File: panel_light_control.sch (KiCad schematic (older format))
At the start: 61 parts, among them J1 Conn_01x02, J6 Conn_01x04, Q1 IRF540N, Q2 IRF540N, U1 L7805, U2 LM324, U6 LM324, U7 LM324

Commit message: PHY routing done? Current sink routing is back to square one (yay fwd annotations)
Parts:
- added D4: D, Diode_SMD:D_SMA, symbol Device:D
- D1, D2: footprint Diode_SMD:D_0603_1608Metric -> Diode_SMD:D_SMA; MPN (none) -> CGRA4004-G; Mouser (none) -> 750-CGRA4004-G
- SPI0: value Conn_01x09 -> Conn_01x10; footprint Connector_JST:JST_PH_S9B-PH-K_1x09_P2.00mm_Horizontal -> Connector_JST:JST_PH_S11B-PH-K_1x11_P2.00mm_Horizontal
- renumbered U7 to U2, U6 to U2
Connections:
- wire segments 231 -> 237
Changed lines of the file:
@@
 F 0 "D1" H 3400 1416 50  0000 C CNN
 F 1 "D" H 3400 1325 50  0000 C CNN
-F 2 "Diode_SMD:D_0603_1608Metric" H 3400 1200 50  0001 C CNN
+F 2 "Diode_SMD:D_SMA" H 3400 1200 50  0001 C CNN
 F 3 "~" H 3400 1200 50  0001 C CNN
+F 4 "CGRA4004-G" H 3400 1200 50  0001 C CNN "MPN"
+F 5 "750-CGRA4004-G" H 3400 1200 50  0001 C CNN "Mouser"
 	1    3400 1200
 	1    0    0    -1
@@
 F 0 "D2" H 3400 2400 50  0000 C CNN
 F 1 "D" H 3400 2500 50  0000 C CNN
-F 2 "Diode_SMD:D_0603_1608Metric" H 3400 2600 50  0001 C CNN
+F 2 "Diode_SMD:D_SMA" H 3400 2600 50  0001 C CNN
 F 3 "~" H 3400 2600 50  0001 C CNN
+F 4 "CGRA4004-G" H 3400 2600 50  0001 C CNN "MPN"
+F 5 "750-CGRA4004-G" H 3400 2600 50  0001 C CNN "Mouser"
 	1    3400 2600
 	1    0    0    1
@@
 U 1 1 5C1B802D
 P 4950 1500
-F 0 "U1" H 4950 1742 50  0000 C CNN
-F 1 "L7805" H 4950 1651 50  0000 C CNN
+F 0 "U1" H 5250 1400 50  0000 C CNN
+F 1 "L7805" H 4950 1650 50  0000 C CNN
 F 2 "Package_TO_SOT_THT:TO-220-3_Vertical" H 4975 1350 50  0001 L CIN
 F 3 "http://www.st.com/content/ccc/resource/technical/document/datasheet/41/4f/b3/b0/12/d4/47/88/CD00000444.pdf/files/CD00000444.pdf/jcr:content/translations/en.CD00000444.pdf" H 4950 1450 50  0001 C CNN
@@
 $EndComp
 Wire Wire Line
-	3950 1500 4650 1500
+	3950 1500 4550 1500
 $Comp
 L power:GND #PWR0101
@@
 	5350 1500 5250 1500
 Wire Wire Line
-	5650 1500 5350 1500
+	5650 1500 5550 1500
 Connection ~ 5350 1500
 Text GLabel 10250 2950 0    50   Output ~ 0
@@
 P 10600 4900
 F 0 "SPI0" H 10680 4892 50  0000 L CNN
-F 1 "Conn_01x09" H 10680 4801 50  0000 L CNN
-F 2 "Connector_JST:JST_PH_S9B-PH-K_1x09_P2.00mm_Horizontal" H 10600 4900 50  0001 C CNN
+F 1 "Conn_01x10" H 10680 4801 50  0000 L CNN
+F 2 "Connector_JST:JST_PH_S11B-PH-K_1x11_P2.00mm_Horizontal" H 10600 4900 50  0001 C CNN
 F 3 "~" H 10600 4900 50  0001 C CNN
 	1    10600 4900
@@
 L power:PWR_FLAG #FLG0104
 U 1 1 5C1C5DD8
-P 5350 1400
-F 0 "#FLG0104" H 5350 1475 50  0001 C CNN
-F 1 "PWR_FLAG" H 5350 1574 50  0000 C CNN
-F 2 "" H 5350 1400 50  0001 C CNN
-F 3 "~" H 5350 1400 50  0001 C CNN
-	1    5350 1400
-	1    0    0    -1
-$EndComp
-Wire Wire Line
-	5350 1400 5350 1500
+P 5550 1400
+F 0 "#FLG0104" H 5550 1475 50  0001 C CNN
+F 1 "PWR_FLAG" H 5550 1574 50  0000 C CNN
+F 2 "" H 5550 1400 50  0001 C CNN
+F 3 "~" H 5550 1400 50  0001 C CNN
+	1    5550 1400
+	1    0    0    -1
+$EndComp
 Wire Wire Line
 	2800 1500 2800 2600
@@
 	8950 4500 8950 4600
 $Comp
-L Amplifier_Operational:LM324 U7
-U 2 1 5CE1E150
+L Amplifier_Operational:LM324 U2
+U 3 1 5CE1E150
 P 7750 5400
-F 0 "U7" H 7750 5600 50  0000 C CNN
+F 0 "U2" H 7750 5600 50  0000 C CNN
 F 1 "LM324" H 7700 5400 50  0000 C CNN
 F 2 "Package_DIP:DIP-14_W7.62mm_Socket" H 7700 5500 50  0001 C CNN
 F 3 "http://www.ti.com/lit/ds/symlink/lm2902-n.pdf" H 7800 5600 50  0001 C CNN
-	2    7750 5400
+	3    7750 5400
 	1    0    0    -1
 $EndComp
@@
 	8950 6100 8950 6200
 $Comp
-L Amplifier_Operational:LM324 U6
-U 2 1 5CE38662
+L Amplifier_Operational:LM324 U2
+U 1 1 5CE38662
 P 7750 2250
-F 0 "U6" H 7750 2450 50  0000 C CNN
+F 0 "U2" H 7750 2450 50  0000 C CNN
 F 1 "LM324" H 7700 2250 50  0000 C CNN
 F 2 "Package_DIP:DIP-14_W7.62mm_Socket" H 7700 2350 50  0001 C CNN
 F 3 "http://www.ti.com/lit/ds/symlink/lm2902-n.pdf" H 7800 2450 50  0001 C CNN
-	2    7750 2250
+	1    7750 2250
 	1    0    0    -1
 $EndComp
@@
 Wire Wire Line
 	8950 2950 8950 3050
+Wire Wire Line
+	5550 1400 5550 1500
+Connection ~ 5550 1500
+Wire Wire Line
+	5550 1500 5350 1500
+Wire Wire Line
+	4800 1200 4550 1200
+Wire Wire Line
+	4550 1200 4550 1500
+Connection ~ 4550 1500
+Wire Wire Line
+	4550 1500 4650 1500
+Wire Wire Line
+	5100 1200 5350 1200
+Wire Wire Line
+	5350 1200 5350 1500
+$Comp
+L Device:D D4
+U 1 1 5BD4F72E
+P 4950 1200
+F 0 "D4" H 4950 1416 50  0000 C CNN
+F 1 "D" H 4950 1325 50  0000 C CNN
+F 2 "Diode_SMD:D_SMA" H 4950 1200 50  0001 C CNN
+F 3 "~" H 4950 1200 50  0001 C CNN
+F 4 "CGRA4004-G" H 4950 1200 50  0001 C CNN "MPN"
+F 5 "750-CGRA4004-G" H 4950 1200 50  0001 C CNN "Mouser"
+	1    4950 1200
+	1    0    0    -1
+$EndComp
 $EndSCHEMATC

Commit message: further re-arrangement, PCB is now 100x90 mm² \o/. A bit more placement to do, then back to routing :>
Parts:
- removed C13, C14: 4.7uF, Capacitor_SMD:C_1206_3216Metric, symbol Device:C
- removed C2: 100nF, Capacitor_SMD:C_0603_1608Metric, symbol Device:C
- removed D3: D_Small, Diode_SMD:D_0603_1608Metric, symbol Device:D_Small
- added C25, C41, C42, C43: 22µF, Capacitor_SMD:C_1210_3225Metric, symbol Device:C
- added C38, C39, C40: 100nF, Capacitor_SMD:C_0603_1608Metric, symbol Device:C
- added D3: 1D4004, Diode_SMD:D_SMA, symbol Device:D
- added L2, L3: 4.7µH, Inductor_SMD:L_Taiyo-Yuden_NR-50xx, symbol Device:L
- C3: value 47uF -> 22µF; footprint Capacitor_SMD:C_0603_1608Metric -> Capacitor_SMD:C_1210_3225Metric; MPN (none) -> GMK325BJ226MM-P; Mouser (none) -> 963-GMK325BJ226MM-P
- D1, D2, D4: value D -> 1D4004
- PS1: Mouser (none) -> 919-R-78B12-2.0
- PS2: Arrow Part Number R-78B5.0-1.0 -> (none); Arrow Price/Stock https://www.arrow.com/en/products/r-78b5.0-1.0/recom-power -> (none); Description Switching Regulator R-78B5.0-1.0, 5V 1A Switching Regulator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 -> Non-Isolated DC/DC Converters 1A DC/DC REG 4.75-34Vin 3.3Vou; MPN (none) -> R-78B3.3-1.0; Manufacturer_Name RECOM Power -> (none); Manufacturer_Part_Number R-78B5.0-1.0 -> (none); Mouser (none) -> 919-R-78B3.3-1.0; RS Part Number 1668746 -> (none); RS Price/Stock http://uk.rs-online.com/web/p/products/1668746 -> (none)
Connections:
- wire segments 237 -> 252
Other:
- moved on the sheet: C12, C3, C6, C7, D1, D2, D4, F1, J1, PS1, PS2, PS3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

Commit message: Tweaked MOSFET sink layout. Changed LM324 to SOIC.
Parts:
- U2: footprint Package_DIP:DIP-14_W7.62mm_Socket -> Package_SO:SOIC-14_3.9x8.7mm_P1.27mm
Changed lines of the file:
@@
 EESchema Schematic File Version 4
 LIBS:panel_light_control-cache
-EELAYER 28 0
+EELAYER 26 0
 EELAYER END
 $Descr A4 11693 8268
@@
 F 0 "U2" H 8408 1046 50  0000 L CNN
 F 1 "LM324" H 8408 955 50  0000 L CNN
-F 2 "Package_DIP:DIP-14_W7.62mm_Socket" H 8400 1100 50  0001 C CNN
+F 2 "Package_SO:SOIC-14_3.9x8.7mm_P1.27mm" H 8400 1100 50  0001 C CNN
 F 3 "http://www.ti.com/lit/ds/symlink/lm2902-n.pdf" H 8500 1200 50  0001 C CNN
 	5    8450 1000
@@
 F 0 "U2" H 7750 1300 50  0000 C CNN
 F 1 "LM324" H 7700 1100 50  0000 C CNN
-F 2 "Package_DIP:DIP-14_W7.62mm_Socket" H 7700 1200 50  0001 C CNN
+F 2 "Package_SO:SOIC-14_3.9x8.7mm_P1.27mm" H 7700 1200 50  0001 C CNN
 F 3 "http://www.ti.com/lit/ds/symlink/lm2902-n.pdf" H 7800 1300 50  0001 C CNN
 	4    7750 1100
@@
 F 0 "U2" H 7750 4000 50  0000 C CNN
 F 1 "LM324" H 7700 3800 50  0000 C CNN
-F 2 "Package_DIP:DIP-14_W7.62mm_Socket" H 7700 3900 50  0001 C CNN
+F 2 "Package_SO:SOIC-14_3.9x8.7mm_P1.27mm" H 7700 3900 50  0001 C CNN
 F 3 "http://www.ti.com/lit/ds/symlink/lm2902-n.pdf" H 7800 4000 50  0001 C CNN
 	2    7750 3800
@@
 F 0 "U2" H 7750 5600 50  0000 C CNN
 F 1 "LM324" H 7700 5400 50  0000 C CNN
-F 2 "Package_DIP:DIP-14_W7.62mm_Socket" H 7700 5500 50  0001 C CNN
+F 2 "Package_SO:SOIC-14_3.9x8.7mm_P1.27mm" H 7700 5500 50  0001 C CNN
 F 3 "http://www.ti.com/lit/ds/symlink/lm2902-n.pdf" H 7800 5600 50  0001 C CNN
 	3    7750 5400
@@
 F 0 "U2" H 7750 2450 50  0000 C CNN
 F 1 "LM324" H 7700 2250 50  0000 C CNN
-F 2 "Package_DIP:DIP-14_W7.62mm_Socket" H 7700 2350 50  0001 C CNN
+F 2 "Package_SO:SOIC-14_3.9x8.7mm_P1.27mm" H 7700 2350 50  0001 C CNN
 F 3 "http://www.ti.com/lit/ds/symlink/lm2902-n.pdf" H 7800 2450 50  0001 C CNN
 	1    7750 2250
@@
 Connection ~ 2600 2300
 $Comp
-L power:GND #PWR?
+L power:GND #PWR0113
 U 1 1 5C2605FC
 P 7100 4650
-F 0 "#PWR?" H 7100 4400 50  0001 C CNN
+F 0 "#PWR0113" H 7100 4400 50  0001 C CNN
 F 1 "GND" H 7105 4477 50  0000 C CNN
 F 2 "" H 7100 4650 50  0001 C CNN

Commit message: Add LEDs, tweak MOSFET sink.
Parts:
- R17, R18, R6: footprint Resistor_SMD:R_0603_1608Metric -> Resistor_SMD:R_1206_3216Metric
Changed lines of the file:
@@
 F 0 "R17" H 9150 4400 50  0000 C CNN
 F 1 "0.22" H 9150 4300 50  0000 C CNN
-F 2 "Resistor_SMD:R_0603_1608Metric" V 8880 4350 50  0001 C CNN
+F 2 "Resistor_SMD:R_1206_3216Metric" V 8880 4350 50  0001 C CNN
 F 3 "~" H 8950 4350 50  0001 C CNN
 	1    8950 4350
@@
 F 0 "R18" H 9150 6000 50  0000 C CNN
 F 1 "0.22" H 9150 5900 50  0000 C CNN
-F 2 "Resistor_SMD:R_0603_1608Metric" V 8880 5950 50  0001 C CNN
+F 2 "Resistor_SMD:R_1206_3216Metric" V 8880 5950 50  0001 C CNN
 F 3 "~" H 8950 5950 50  0001 C CNN
 	1    8950 5950
@@
 F 0 "R6" H 9150 2850 50  0000 C CNN
 F 1 "0.22" H 9150 2750 50  0000 C CNN
-F 2 "Resistor_SMD:R_0603_1608Metric" V 8880 2800 50  0001 C CNN
+F 2 "Resistor_SMD:R_1206_3216Metric" V 8880 2800 50  0001 C CNN
 F 3 "~" H 8950 2800 50  0001 C CNN
 	1    8950 2800
@@
 	4600 1200 4300 1200
 Connection ~ 2600 2300
-$Comp
-L power:GND #PWR0113
-U 1 1 5C2605FC
-P 7100 4650
-F 0 "#PWR0113" H 7100 4400 50  0001 C CNN
-F 1 "GND" H 7105 4477 50  0000 C CNN
-F 2 "" H 7100 4650 50  0001 C CNN
-F 3 "" H 7100 4650 50  0001 C CNN
-	1    7100 4650
-	1    0    0    -1
-$EndComp
-Wire Wire Line
-	7100 4550 7100 4650
 Wire Wire Line
 	1700 1200 2000 1200

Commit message: 3.3V buck converter now connected to 12V (prep for 48V>12V upgrade regarding IoP applicability)
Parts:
- added D5: LED_SYSTEM, LED_SMD:LED_Cree-PLCC4_2x2mm_CW, symbol Device:LED_RCBG
- added R39: 220R, Resistor_SMD:R_0603_1608Metric, symbol Device:R_Small
- added R40, R41: 1k, Resistor_SMD:R_0603_1608Metric, symbol Device:R_Small
- F1: value Polyfuse_Small -> Polyfuse 3A; footprint Fuse:Fuse_2512_6332Metric -> SamacSys_Parts:30R400UF; MPN (none) -> 30R300UU; Mouser (none) -> 576-30R300UU
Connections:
- net +12V: now also L2.1
- net +24V: no longer L2.1
- net GND: now also D5.2 (K)
- net PWM_B: now also R39.2
- net PWM_G: now also R40.2
- net PWM_R: now also R41.2
- new net: D5.1 (RA), R41.1
- new net: D5.3 (BA), R39.1
- new net: D5.4 (GA), R40.1
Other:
- moved on the sheet: C39, C41, C7, D2, L2, PS2, PS3, PS4

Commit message: two sections left to place: 3ch current sink, microcontroller area. Todo: * find proper barrel jacks, spec MPN, Mouser * add status LEDs to the LDD-H outputs * add 7th LED for funsies :> * swap LM324 units around until everything lines up best
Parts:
- U2: MPN (none) -> LM324ADR; Mouser (none) -> 595-LM324ADR
- renumbered G3 to Q3
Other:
- moved on the sheet: L3
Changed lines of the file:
@@
 F 2 "Package_SO:SOIC-14_3.9x8.7mm_P1.27mm" H 7700 1200 50  0001 C CNN
 F 3 "http://www.ti.com/lit/ds/symlink/lm2902-n.pdf" H 7800 1300 50  0001 C CNN
+F 4 "LM324ADR" H 7750 1100 50  0001 C CNN "MPN"
+F 5 "595-LM324ADR" H 7750 1100 50  0001 C CNN "Mouser"
 	4    7750 1100
 	1    0    0    -1
@@
 F 2 "Package_SO:SOIC-14_3.9x8.7mm_P1.27mm" H 7700 3900 50  0001 C CNN
 F 3 "http://www.ti.com/lit/ds/symlink/lm2902-n.pdf" H 7800 4000 50  0001 C CNN
+F 4 "LM324ADR" H 7750 3800 50  0001 C CNN "MPN"
+F 5 "595-LM324ADR" H 7750 3800 50  0001 C CNN "Mouser"
 	2    7750 3800
 	1    0    0    -1
@@
 F 2 "Package_SO:SOIC-14_3.9x8.7mm_P1.27mm" H 7700 5500 50  0001 C CNN
 F 3 "http://www.ti.com/lit/ds/symlink/lm2902-n.pdf" H 7800 5600 50  0001 C CNN
+F 4 "LM324ADR" H 7750 5400 50  0001 C CNN "MPN"
+F 5 "595-LM324ADR" H 7750 5400 50  0001 C CNN "Mouser"
 	3    7750 5400
 	1    0    0    -1
@@
 $EndComp
 $Comp
-L Transistor_FET:IRF540N G3
+L Transistor_FET:IRF540N Q3
 U 1 1 5CE1E180
 P 8850 5400
-F 0 "G3" H 9055 5446 50  0000 L CNN
+F 0 "Q3" H 9055 5446 50  0000 L CNN
 F 1 "IRF540N" H 9055 5355 50  0000 L CNN
 F 2 "Package_TO_SOT_THT:TO-220-3_Vertical" H 9100 5325 50  0001 L CIN
@@
 F 2 "Package_SO:SOIC-14_3.9x8.7mm_P1.27mm" H 7700 2350 50  0001 C CNN
 F 3 "http://www.ti.com/lit/ds/symlink/lm2902-n.pdf" H 7800 2450 50  0001 C CNN
+F 4 "LM324ADR" H 7750 2250 50  0001 C CNN "MPN"
+F 5 "595-LM324ADR" H 7750 2250 50  0001 C CNN "Mouser"
 	1    7750 2250
 	1    0    0    -1
@@
 $EndComp
 Wire Wire Line
-	2950 1200 3000 1200
+	2800 1200 3000 1200
 $Comp
 L Device:C C42
@@
 L Device:L L3
 U 1 1 5BFEC541
-P 2800 1200
-F 0 "L3" V 2990 1200 50  0000 C CNN
-F 1 "4.7µH" V 2899 1200 50  0000 C CNN
-F 2 "Inductor_SMD:L_Taiyo-Yuden_NR-50xx" H 2800 1200 50  0001 C CNN
-F 3 "~" H 2800 1200 50  0001 C CNN
-F 4 "VLS5045EX-4R7M-CA " H 2800 1200 50  0001 C CNN "MPN"
-F 5 "810-VLS5045EX4R7MCA" H 2800 1200 50  0001 C CNN "Mouser"
-	1    2800 1200
+P 2650 1200
+F 0 "L3" V 2840 1200 50  0000 C CNN
+F 1 "4.7µH" V 2749 1200 50  0000 C CNN
+F 2 "Inductor_SMD:L_Taiyo-Yuden_NR-50xx" H 2650 1200 50  0001 C CNN
+F 3 "~" H 2650 1200 50  0001 C CNN
+F 4 "VLS5045EX-4R7M-CA " H 2650 1200 50  0001 C CNN "MPN"
+F 5 "810-VLS5045EX4R7MCA" H 2650 1200 50  0001 C CNN "Mouser"
+	1    2650 1200
 	0    -1   -1   0
 $EndComp
@@
 	1700 1700 2000 1700
 Wire Wire Line
-	2300 1200 2650 1200
+	2300 1200 2500 1200
 Text GLabel 2800 2350 0    50   Input ~ 0
 +12V

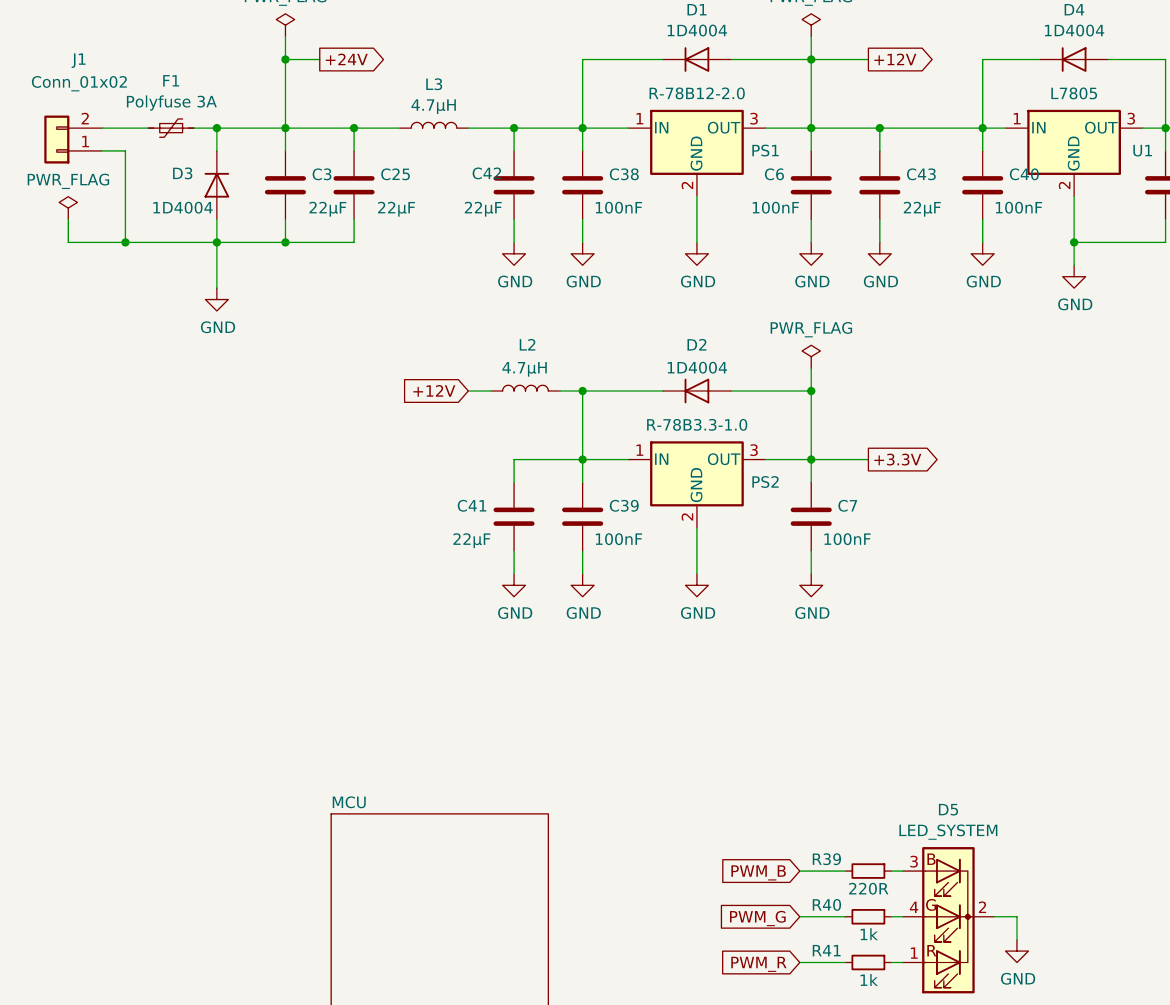
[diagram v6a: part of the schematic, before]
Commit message: THT pad restring sizes increase for mechanical stability; generalized LED arrangement for more flexibility (8 bit display, CAN LED, PWM and general purpose RGB) and development-style look and feel; protection diode footprint is now THT to reduce reworking hassle should it short out due to misuse
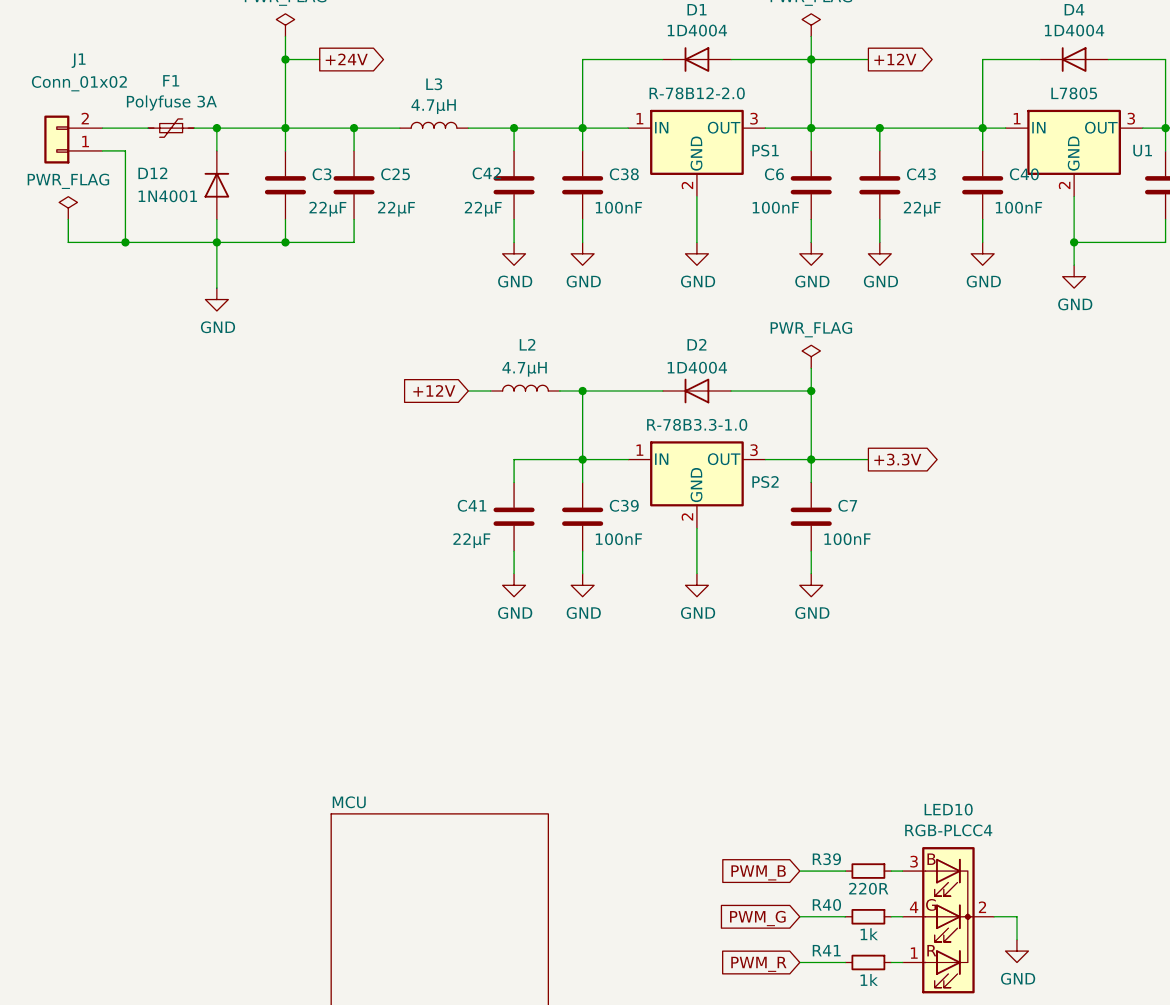
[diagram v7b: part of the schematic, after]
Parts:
- removed D3: 1D4004, Diode_SMD:D_SMA, symbol Device:D
- added D12: 1N4001, Diode_THT:D_DO-41_SOD81_P3.81mm_Vertical_AnodeUp, symbol Diode:1N4001
- LED10: renamed from D5; value LED_SYSTEM -> RGB-PLCC4
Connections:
- net +24V: now also D12.1 (K)
- net GND: now also D12.2 (A)
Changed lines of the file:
@@
 	1    0    0    -1
-$EndComp
-$Comp
-L Device:D D3
-U 1 1 5BDA8380
-P 1700 1450
-F 0 "D3" V 1650 1600 50  0000 C CNN
-F 1 "1D4004" V 1800 1600 50  0000 C CNN
-F 2 "Diode_SMD:D_SMA" H 1700 1450 50  0001 C CNN
-F 3 "~" H 1700 1450 50  0001 C CNN
-F 4 "CGRA4004-G" H 1700 1450 50  0001 C CNN "MPN"
-F 5 "750-CGRA4004-G" H 1700 1450 50  0001 C CNN "Mouser"
-	1    1700 1450
-	0    -1   1    0
 $EndComp
 Wire Wire Line
@@
 P 4900 4650
 AR Path="/5BBC4BB7/5BE88702" Ref="D?"  Part="1"
-AR Path="/5BE88702" Ref="D5"  Part="1"
-F 0 "D5" H 4900 4183 50  0000 C CNN
-F 1 "LED_SYSTEM" H 4900 4274 50  0000 C CNN
+AR Path="/5BE88702" Ref="LED10"  Part="1"
+F 0 "LED10" H 4900 4183 50  0000 C CNN
+F 1 "RGB-PLCC4" H 4900 4274 50  0000 C CNN
 F 2 "LED_SMD:LED_Cree-PLCC4_2x2mm_CW" H 4900 4600 50  0001 C CNN
 F 3 "~" H 4900 4600 50  0001 C CNN
@@
 Text GLabel 4250 4450 0    50   Input ~ 0
 PWM_B
+$Comp
+L Diode:1N4001 D12
+U 1 1 5BD0EDAE
+P 1700 1450
+F 0 "D12" V 1650 1800 50  0000 R CNN
+F 1 "1N4001" V 1750 1800 50  0000 R CNN
+F 2 "Diode_THT:D_DO-41_SOD81_P3.81mm_Vertical_AnodeUp" H 1700 1275 50  0001 C CNN
+F 3 "http://www.vishay.com/docs/88503/1n4001.pdf" H 1700 1450 50  0001 C CNN
+	1    1700 1450
+	0    -1   1    0
+$EndComp
 $EndSCHEMATC

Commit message: R-78B3.3 footprint fixed (had the E version -> mirrored), next: place remaining current sink circuit parts, route upper half of the PCB, tidy up CAN placement, verify µC pin mapping again, route lower half :)
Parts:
- PS2: footprint Converter_DCDC:Converter_DCDC_RECOM_R-78E-0.5_THT -> Converter_DCDC:Converter_DCDC_RECOM_R-78B-2.0_THT; symbol Regulator_Switching:R-783.3-1.0 -> Regulator_Switching:R-78B3.3-2.0
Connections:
- net GND: now also U2.10 (+); no longer U2.12 (+)
- net at C8.2, R7.1, R8.1: now also U2.3 (+); no longer U2.5 (+)
- net at C10.2, R11.1, R14.1: now also U2.2 (-); no longer U2.6 (-)
- net at C10.1, R13.2: now also U2.1; no longer U2.7
- net at C9.2, R10.1, R9.1: now also U2.5 (+); no longer U2.10 (+)
- net at C11.1, R15.2: now also U2.7; no longer U2.8
- net at C11.2, R12.1, R16.1: now also U2.6 (-); no longer U2.9 (-)
- net at C4.1, R4.2: now also U2.14; no longer U2.1
- net at C4.2, R3.1, R5.1: now also U2.13 (-); no longer U2.2 (-)
- net at C1.2, R1.1, R2.1: now also U2.12 (+); no longer U2.3 (+)
- new net: U2.8, U2.9 (-)
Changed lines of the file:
@@
 $EndComp
 $Comp
-L Regulator_Switching:R-783.3-1.0 PS2
+L Regulator_Switching:R-78B3.3-2.0 PS2
 U 1 1 5BB90449
 P 3800 2650
 F 0 "PS2" H 4100 2550 50  0000 C CNN
 F 1 "R-78B3.3-1.0" H 3800 2800 50  0000 C CNN
-F 2 "Converter_DCDC:Converter_DCDC_RECOM_R-78E-0.5_THT" H 4850 2750 50  0001 L CNN
+F 2 "Converter_DCDC:Converter_DCDC_RECOM_R-78B-2.0_THT" H 4850 2750 50  0001 L CNN
 F 3 "" H 4850 2650 50  0001 L CNN
 F 4 "Non-Isolated DC/DC Converters 1A DC/DC REG 4.75-34Vin 3.3Vou" H 4850 2550 50  0001 L CNN "Description"
@@
 $Comp
 L Amplifier_Operational:LM324 U2
-U 4 1 5BC3AA2E
+U 3 1 5BC3AA2E
 P 7750 1100
 F 0 "U2" H 7750 1300 50  0000 C CNN
@@
 F 4 "LM324ADR" H 7750 1100 50  0001 C CNN "MPN"
 F 5 "595-LM324ADR" H 7750 1100 50  0001 C CNN "Mouser"
-	4    7750 1100
+	3    7750 1100
 	1    0    0    -1
 $EndComp
@@
 $Comp
 L Amplifier_Operational:LM324 U2
-U 2 1 5BCB6EE3
+U 1 1 5BCB6EE3
 P 7750 3800
 F 0 "U2" H 7750 4000 50  0000 C CNN
@@
 F 4 "LM324ADR" H 7750 3800 50  0001 C CNN "MPN"
 F 5 "595-LM324ADR" H 7750 3800 50  0001 C CNN "Mouser"
-	2    7750 3800
+	1    7750 3800
 	1    0    0    -1
 $EndComp
@@
 $Comp
 L Amplifier_Operational:LM324 U2
-U 3 1 5CE1E150
+U 2 1 5CE1E150
 P 7750 5400
 F 0 "U2" H 7750 5600 50  0000 C CNN
@@
 F 4 "LM324ADR" H 7750 5400 50  0001 C CNN "MPN"
 F 5 "595-LM324ADR" H 7750 5400 50  0001 C CNN "Mouser"
-	3    7750 5400
+	2    7750 5400
 	1    0    0    -1
 $EndComp
@@
 $Comp
 L Amplifier_Operational:LM324 U2
-U 1 1 5CE38662
+U 4 1 5CE38662
 P 7750 2250
 F 0 "U2" H 7750 2450 50  0000 C CNN
@@
 F 4 "LM324ADR" H 7750 2250 50  0001 C CNN "MPN"
 F 5 "595-LM324ADR" H 7750 2250 50  0001 C CNN "Mouser"
-	1    7750 2250
-	1    0    0    -1
-$EndComp
+	4    7750 2250
+	1    0    0    -1
+$EndComp
